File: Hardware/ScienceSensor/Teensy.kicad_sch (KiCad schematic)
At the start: 10 parts

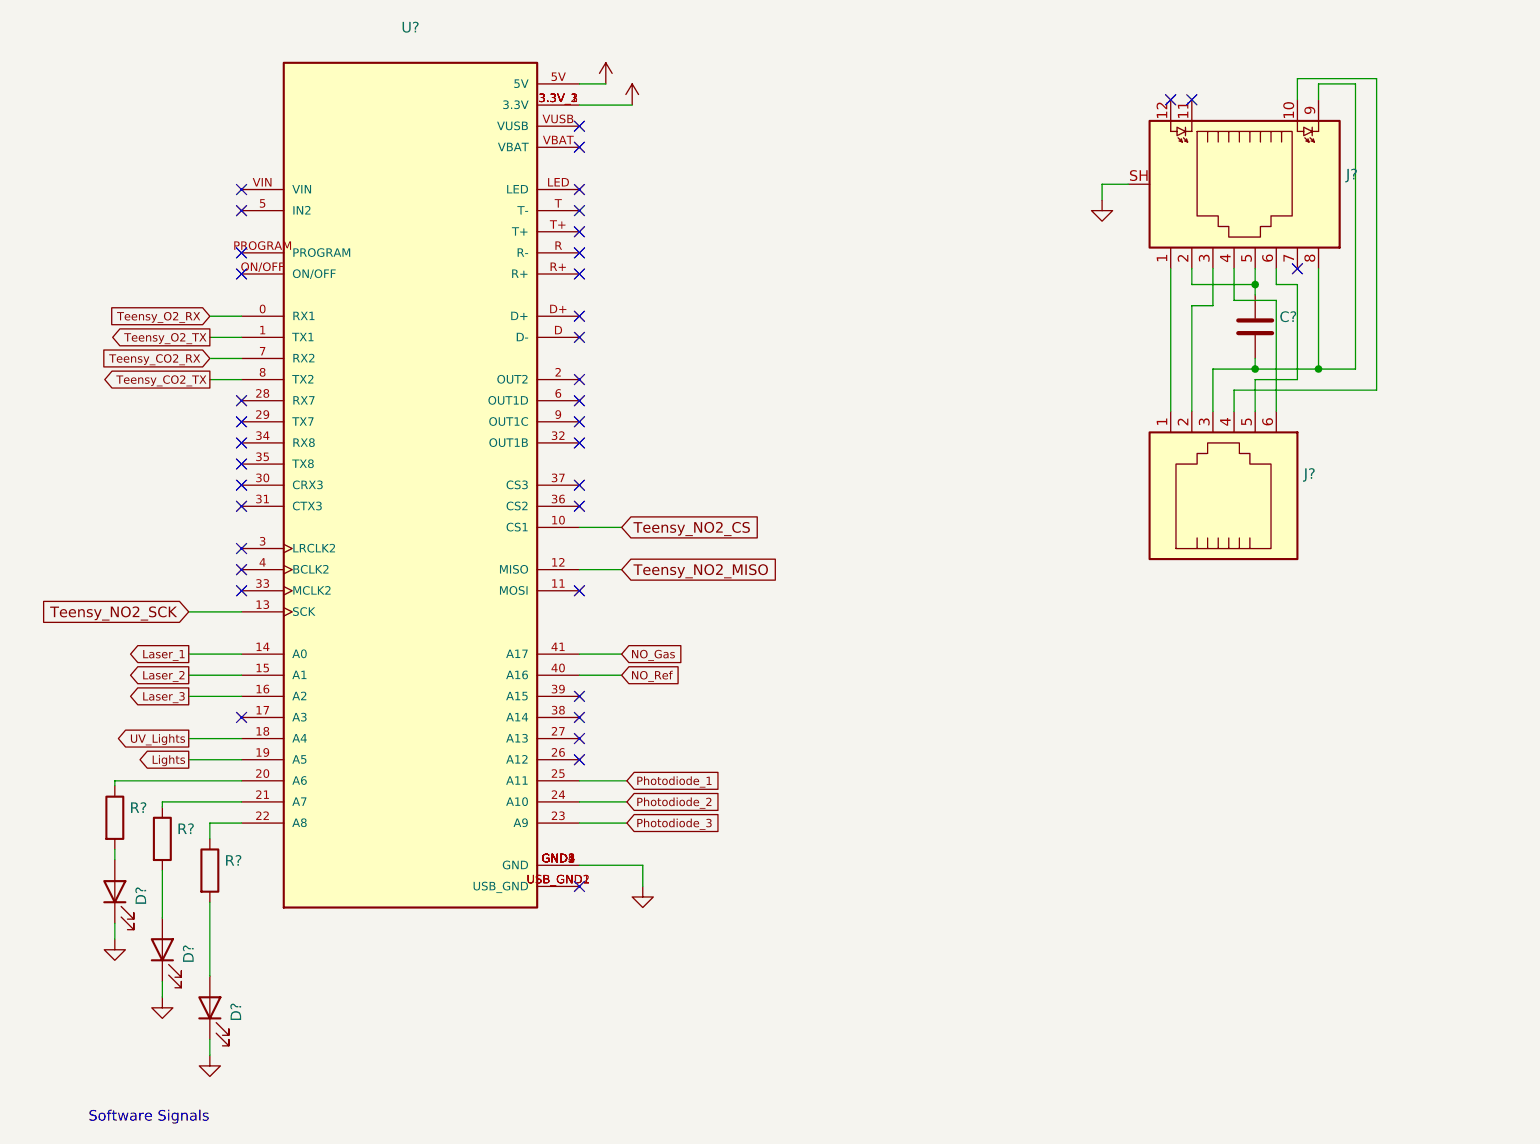
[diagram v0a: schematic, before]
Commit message: Created NO sensor, NH3 sensor, worked on Mosfets, and created Methane sensor with labels.
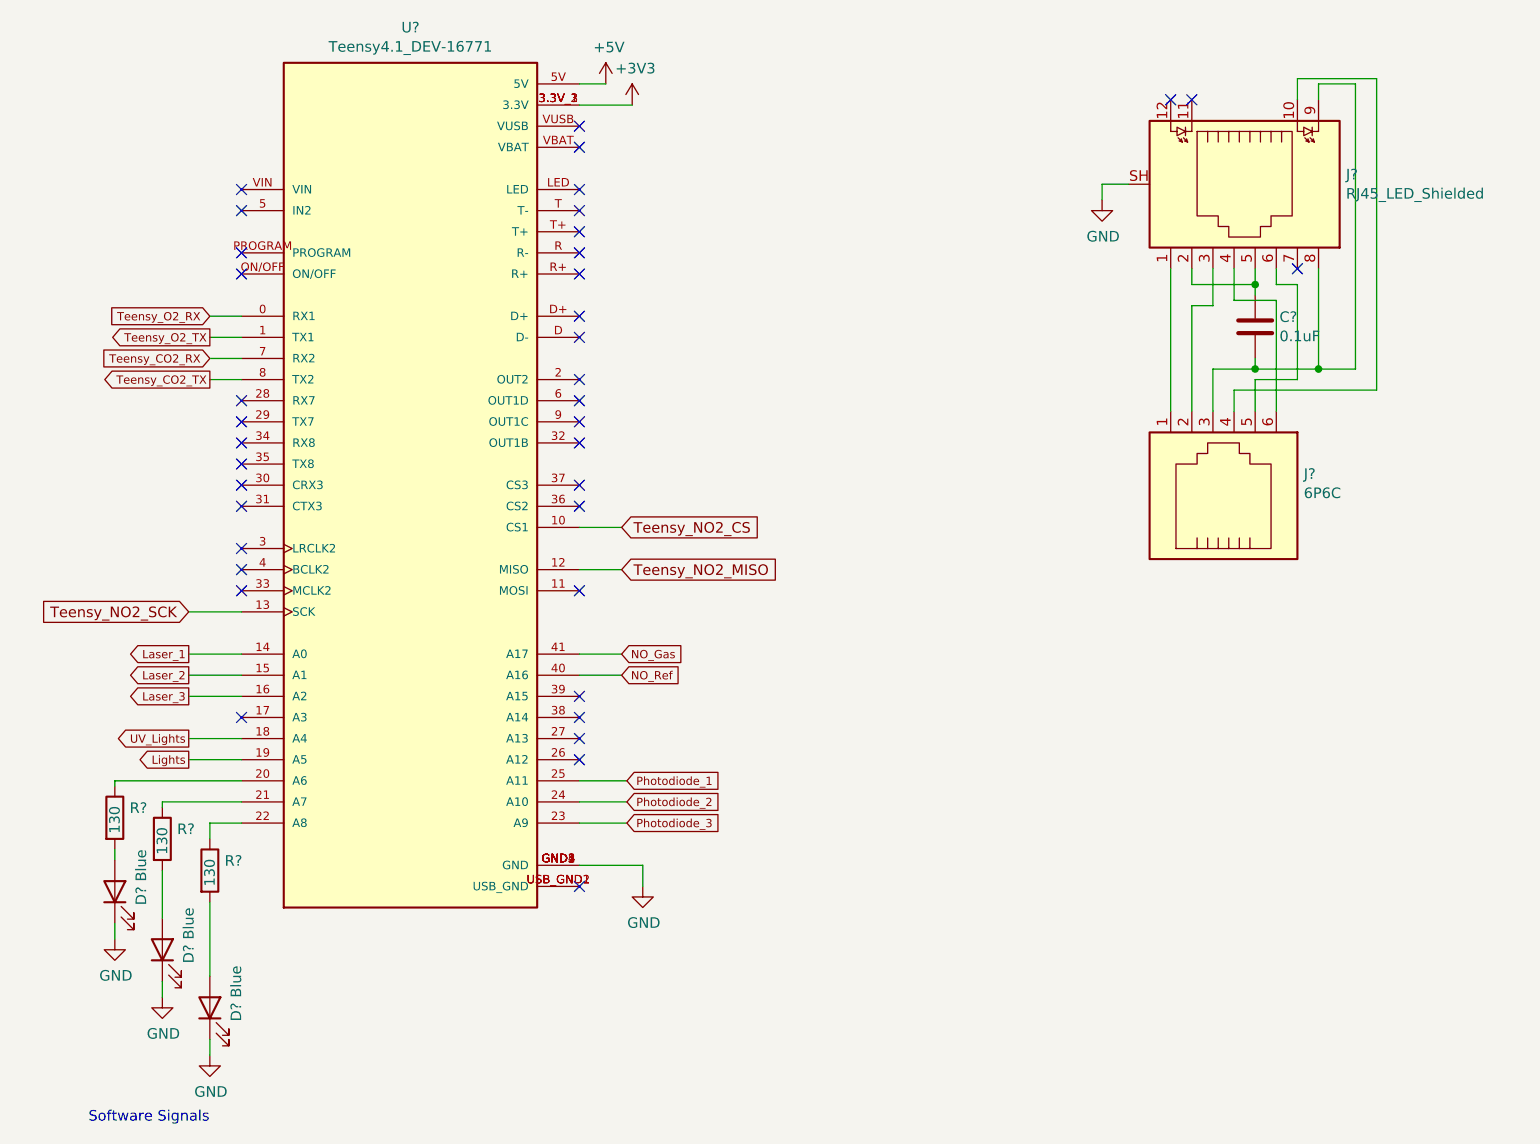
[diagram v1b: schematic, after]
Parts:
- C?: value (none) -> 0.1uF
- D? (x3): value (none) -> Blue
- J?: value (none) -> RJ45_LED_Shielded
- J?: value (none) -> 6P6C
- R? (x3): value (none) -> 130
- U?: value (none) -> Teensy4.1_DEV-16771; footprint (none) -> MODULE_DEV-16771
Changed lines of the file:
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@@
     (in_bom yes) (on_board yes)
     (property "Reference" "U?" (id 0) (at 90.805 33.8582 0))
-    (property "Value" "" (id 1) (at 90.805 36.1696 0))
-    (property "Footprint" "" (id 2) (at 144.145 96.52 0)
+    (property "Value" "Teensy4.1_DEV-16771" (id 1) (at 90.805 36.1696 0))
+    (property "Footprint" "MODULE_DEV-16771" (id 2) (at 144.145 96.52 0)
       (effects (font (size 1.27 1.27)) (justify left bottom) hide)
     )
@@
       (effects (font (size 1.27 1.27)) (justify left))
     )
-    (property "Value" "" (id 1) (at 66.675 137.16 90)
+    (property "Value" "130" (id 1) (at 66.675 137.16 90)
       (effects (font (size 1.27 1.27)) (justify left))
     )
@@
       (effects (font (size 1.27 1.27)) (justify left))
     )
-    (property "Value" "" (id 1) (at 60.96 133.35 90)
+    (property "Value" "130" (id 1) (at 60.96 133.35 90)
       (effects (font (size 1.27 1.27)) (justify left))
     )
@@
       (effects (font (size 1.27 1.27)) (justify left))
     )
-    (property "Value" "" (id 1) (at 55.245 130.81 90)
+    (property "Value" "130" (id 1) (at 55.245 130.81 90)
       (effects (font (size 1.27 1.27)) (justify left))
     )
@@
       (effects (font (size 1.27 1.27)) (justify right))
     )
-    (property "Value" "" (id 1) (at 58.42 132.715 0)
+    (property "Value" "Blue" (id 1) (at 58.42 132.715 0)
       (effects (font (size 1.27 1.27)) (justify right))
     )
@@
       (effects (font (size 1.27 1.27)) (justify right))
     )
-    (property "Value" "" (id 1) (at 69.85 146.685 0)
+    (property "Value" "Blue" (id 1) (at 69.85 146.685 0)
       (effects (font (size 1.27 1.27)) (justify right))
     )
@@
       (effects (font (size 1.27 1.27)) (justify right))
     )
-    (property "Value" "" (id 1) (at 64.135 139.7 0)
+    (property "Value" "Blue" (id 1) (at 64.135 139.7 0)
       (effects (font (size 1.27 1.27)) (justify right))
     )
@@
       (effects (font (size 1.27 1.27)) hide)
     )
-    (property "Value" "" (id 1) (at 66.802 161.8742 0))
+    (property "Value" "GND" (id 1) (at 66.802 161.8742 0))
     (property "Footprint" "" (id 2) (at 66.675 157.48 0)
       (effects (font (size 1.27 1.27)) hide)
@@
       (effects (font (size 1.27 1.27)) hide)
     )
-    (property "Value" "" (id 1) (at 61.087 154.8892 0))
+    (property "Value" "GND" (id 1) (at 61.087 154.8892 0))
     (property "Footprint" "" (id 2) (at 60.96 150.495 0)
       (effects (font (size 1.27 1.27)) hide)
@@
       (effects (font (size 1.27 1.27)) hide)
     )
-    (property "Value" "" (id 1) (at 55.372 147.9042 0))
+    (property "Value" "GND" (id 1) (at 55.372 147.9042 0))
     (property "Footprint" "" (id 2) (at 55.245 143.51 0)
       (effects (font (size 1.27 1.27)) hide)
@@
       (effects (font (size 1.27 1.27)) (justify left))
     )
-    (property "Value" "" (id 1) (at 203.327 53.848 90)
+    (property "Value" "RJ45_LED_Shielded" (id 1) (at 203.327 53.848 90)
       (effects (font (size 1.27 1.27)) (justify left))
     )
@@
       (effects (font (size 1.27 1.27)) (justify left))
     )
-    (property "Value" "" (id 1) (at 198.247 89.8652 90)
+    (property "Value" "6P6C" (id 1) (at 198.247 89.8652 90)
       (effects (font (size 1.27 1.27)) (justify left))
     )
@@
       (effects (font (size 1.27 1.27)) (justify left))
     )
-    (property "Value" "" (id 1) (at 195.326 70.993 0)
+    (property "Value" "0.1uF" (id 1) (at 195.326 70.993 0)
       (effects (font (size 1.27 1.27)) (justify left))
     )
@@
       (effects (font (size 1.27 1.27)) hide)
     )
-    (property "Value" "" (id 1) (at 174.117 59.0042 0))
+    (property "Value" "GND" (id 1) (at 174.117 59.0042 0))
     (property "Footprint" "" (id 2) (at 173.99 54.61 0)
       (effects (font (size 1.27 1.27)) hide)
@@
       (effects (font (size 1.27 1.27)) hide)
     )
-    (property "Value" "" (id 1) (at 114.681 36.2458 0))
+    (property "Value" "+5V" (id 1) (at 114.681 36.2458 0))
     (property "Footprint" "" (id 2) (at 114.3 40.64 0)
       (effects (font (size 1.27 1.27)) hide)
@@
       (effects (font (size 1.27 1.27)) hide)
     )
-    (property "Value" "" (id 1) (at 117.856 38.7858 0))
+    (property "Value" "+3V3" (id 1) (at 117.856 38.7858 0))
     (property "Footprint" "" (id 2) (at 117.475 43.18 0)
       (effects (font (size 1.27 1.27)) hide)
@@
       (effects (font (size 1.27 1.27)) hide)
     )
-    (property "Value" "" (id 1) (at 118.872 141.5542 0))
+    (property "Value" "GND" (id 1) (at 118.872 141.5542 0))
     (property "Footprint" "" (id 2) (at 118.745 137.16 0)
       (effects (font (size 1.27 1.27)) hide)

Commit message: BOM generated, photodiodes added
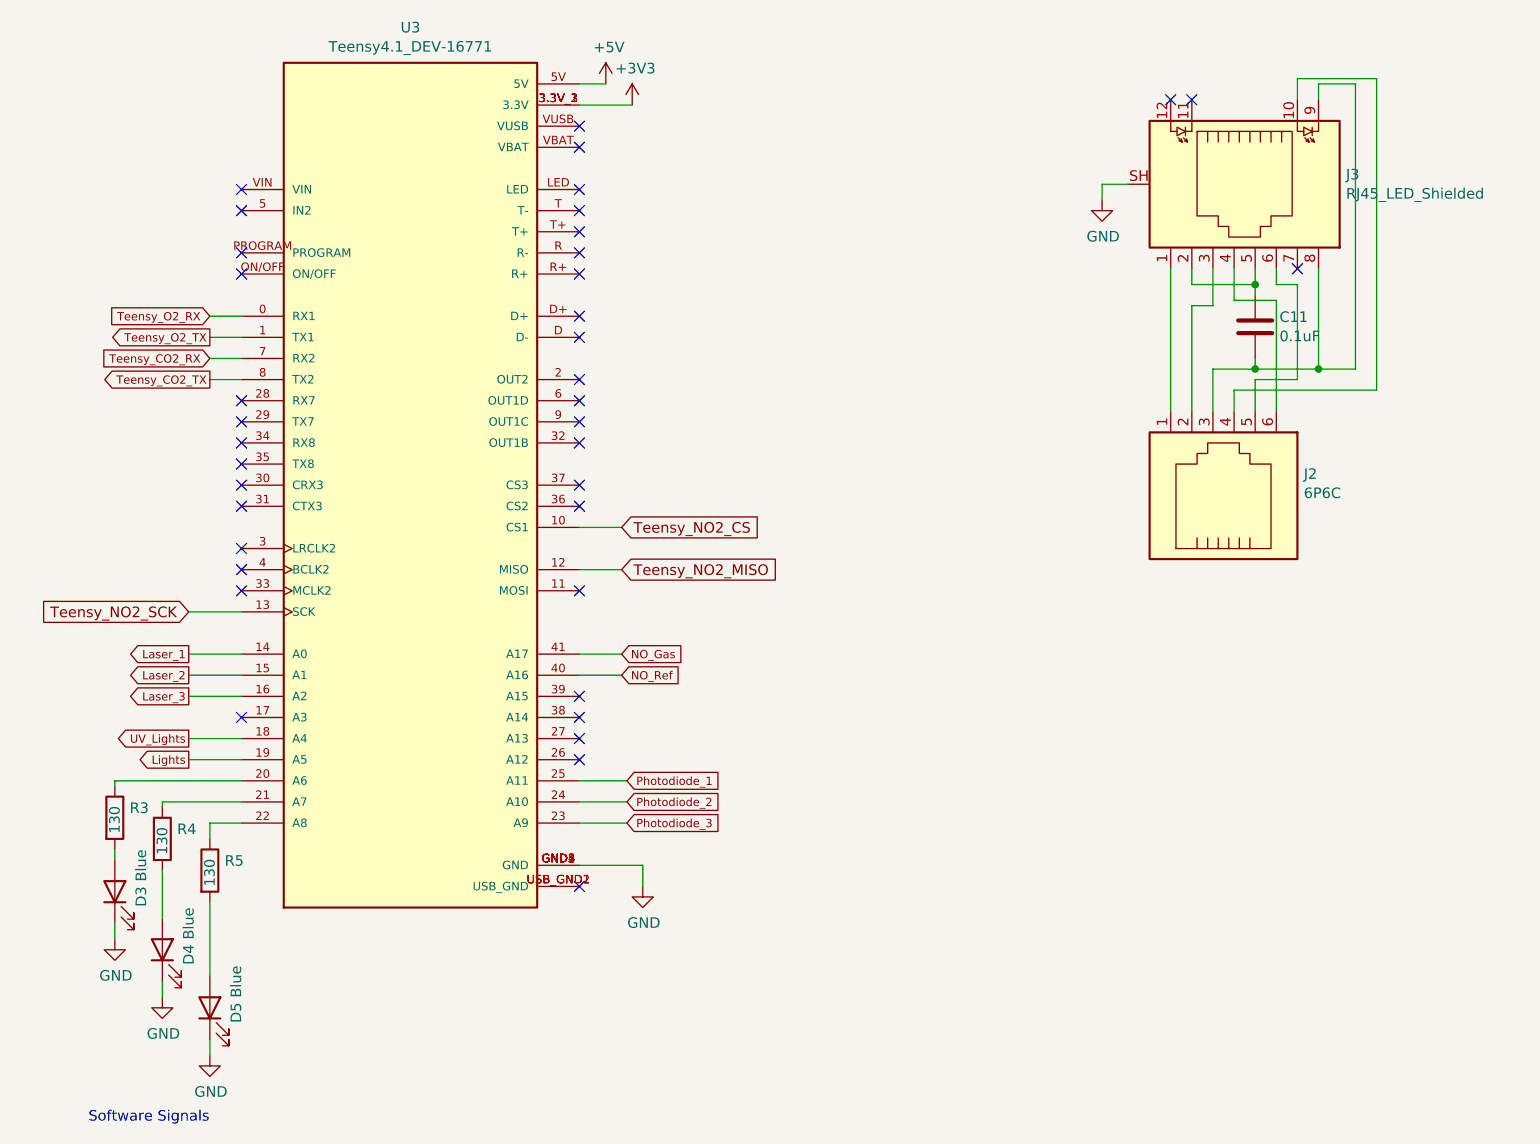
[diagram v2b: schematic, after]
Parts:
- gave numbers to parts that had none: 10
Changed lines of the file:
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@@
   (symbol (lib_id "MRDT_Shields:Teensy4.1_DEV-16771") (at 90.805 88.9 0) (unit 1)
     (in_bom yes) (on_board yes)
-    (property "Reference" "U?" (id 0) (at 90.805 33.8582 0))
+    (property "Reference" "U3" (id 0) (at 90.805 33.8582 0))
     (property "Value" "Teensy4.1_DEV-16771" (id 1) (at 90.805 36.1696 0))
     (property "Footprint" "MODULE_DEV-16771" (id 2) (at 144.145 96.52 0)
@@
   (symbol (lib_id "Device:R") (at 66.675 135.255 0) (unit 1)
     (in_bom yes) (on_board yes)
-    (property "Reference" "R?" (id 0) (at 68.453 134.0866 0)
+    (property "Reference" "R5" (id 0) (at 68.453 134.0866 0)
       (effects (font (size 1.27 1.27)) (justify left))
     )
@@
   (symbol (lib_id "Device:R") (at 60.96 131.445 0) (unit 1)
     (in_bom yes) (on_board yes)
-    (property "Reference" "R?" (id 0) (at 62.738 130.2766 0)
+    (property "Reference" "R4" (id 0) (at 62.738 130.2766 0)
       (effects (font (size 1.27 1.27)) (justify left))
     )
@@
   (symbol (lib_id "Device:R") (at 55.245 128.905 0) (unit 1)
     (in_bom yes) (on_board yes)
-    (property "Reference" "R?" (id 0) (at 57.023 127.7366 0)
+    (property "Reference" "R3" (id 0) (at 57.023 127.7366 0)
       (effects (font (size 1.27 1.27)) (justify left))
     )
@@
   (symbol (lib_id "Device:LED") (at 55.245 137.795 90) (unit 1)
     (in_bom yes) (on_board yes)
-    (property "Reference" "D?" (id 0) (at 58.42 137.16 0)
+    (property "Reference" "D3" (id 0) (at 58.42 137.16 0)
       (effects (font (size 1.27 1.27)) (justify right))
     )
@@
   (symbol (lib_id "Device:LED") (at 66.675 151.765 90) (unit 1)
     (in_bom yes) (on_board yes)
-    (property "Reference" "D?" (id 0) (at 69.85 151.13 0)
+    (property "Reference" "D5" (id 0) (at 69.85 151.13 0)
       (effects (font (size 1.27 1.27)) (justify right))
     )
@@
   (symbol (lib_id "Device:LED") (at 60.96 144.78 90) (unit 1)
     (in_bom yes) (on_board yes)
-    (property "Reference" "D?" (id 0) (at 64.135 144.145 0)
+    (property "Reference" "D4" (id 0) (at 64.135 144.145 0)
       (effects (font (size 1.27 1.27)) (justify right))
     )
@@
   (symbol (lib_id "power:GND") (at 66.675 157.48 0) (unit 1)
     (in_bom yes) (on_board yes)
-    (property "Reference" "#PWR?" (id 0) (at 66.675 163.83 0)
+    (property "Reference" "#PWR039" (id 0) (at 66.675 163.83 0)
       (effects (font (size 1.27 1.27)) hide)
     )
@@
   (symbol (lib_id "power:GND") (at 60.96 150.495 0) (unit 1)
     (in_bom yes) (on_board yes)
-    (property "Reference" "#PWR?" (id 0) (at 60.96 156.845 0)
+    (property "Reference" "#PWR038" (id 0) (at 60.96 156.845 0)
       (effects (font (size 1.27 1.27)) hide)
     )
@@
   (symbol (lib_id "power:GND") (at 55.245 143.51 0) (unit 1)
     (in_bom yes) (on_board yes)
-    (property "Reference" "#PWR?" (id 0) (at 55.245 149.86 0)
+    (property "Reference" "#PWR037" (id 0) (at 55.245 149.86 0)
       (effects (font (size 1.27 1.27)) hide)
     )
@@
   (symbol (lib_id "Connector:RJ45_LED_Shielded") (at 189.865 52.705 270) (unit 1)
     (in_bom yes) (on_board yes)
-    (property "Reference" "J?" (id 0) (at 203.327 51.5366 90)
+    (property "Reference" "J3" (id 0) (at 203.327 51.5366 90)
       (effects (font (size 1.27 1.27)) (justify left))
     )
@@
   (symbol (lib_id "Connector:6P6C") (at 187.325 90.17 270) (mirror x) (unit 1)
     (in_bom yes) (on_board yes)
-    (property "Reference" "J?" (id 0) (at 198.247 87.5538 90)
+    (property "Reference" "J2" (id 0) (at 198.247 87.5538 90)
       (effects (font (size 1.27 1.27)) (justify left))
     )
@@
   (symbol (lib_id "Device:C") (at 192.405 69.85 0) (unit 1)
     (in_bom yes) (on_board yes)
-    (property "Reference" "C?" (id 0) (at 195.326 68.6816 0)
+    (property "Reference" "C11" (id 0) (at 195.326 68.6816 0)
       (effects (font (size 1.27 1.27)) (justify left))
     )
@@
   (symbol (lib_id "power:GND") (at 173.99 54.61 0) (unit 1)
     (in_bom yes) (on_board yes)
-    (property "Reference" "#PWR?" (id 0) (at 173.99 60.96 0)
+    (property "Reference" "#PWR043" (id 0) (at 173.99 60.96 0)
       (effects (font (size 1.27 1.27)) hide)
     )
@@
   (symbol (lib_id "power:+5V") (at 114.3 40.64 0) (unit 1)
     (in_bom yes) (on_board yes)
-    (property "Reference" "#PWR?" (id 0) (at 114.3 44.45 0)
+    (property "Reference" "#PWR040" (id 0) (at 114.3 44.45 0)
       (effects (font (size 1.27 1.27)) hide)
     )
@@
   (symbol (lib_id "power:+3V3") (at 117.475 43.18 0) (unit 1)
     (in_bom yes) (on_board yes)
-    (property "Reference" "#PWR?" (id 0) (at 117.475 46.99 0)
+    (property "Reference" "#PWR041" (id 0) (at 117.475 46.99 0)
       (effects (font (size 1.27 1.27)) hide)
     )
@@
   (symbol (lib_id "power:GND") (at 118.745 137.16 0) (unit 1)
     (in_bom yes) (on_board yes)
-    (property "Reference" "#PWR?" (id 0) (at 118.745 143.51 0)
-      (effects (font (size 1.27 1.27)) hide)
-    )
+    (property "Reference" "#PWR042" (id 0) (at 118.745 143.51 0)
+      (effects (font (size 1.27 1.27)) hide)
+    )
